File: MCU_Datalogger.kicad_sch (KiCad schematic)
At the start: 25 parts, among them U1 24LC1025, U2 DS1337S_, U3 24LC1025, U4 ATMEGA328P-AU, Y1 32.768 KHz, Y2 16MHz

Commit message: Completed Comment
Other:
- note added: "EEPROM"
- note added: "MCU ATMEGA328P"
- note added: "Mounting"
- note added: "RTC DS1377"
- moved on the sheet: BT1, C1, C2, C3, C4, C5, D1, D2, H1, H2, H3, H4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

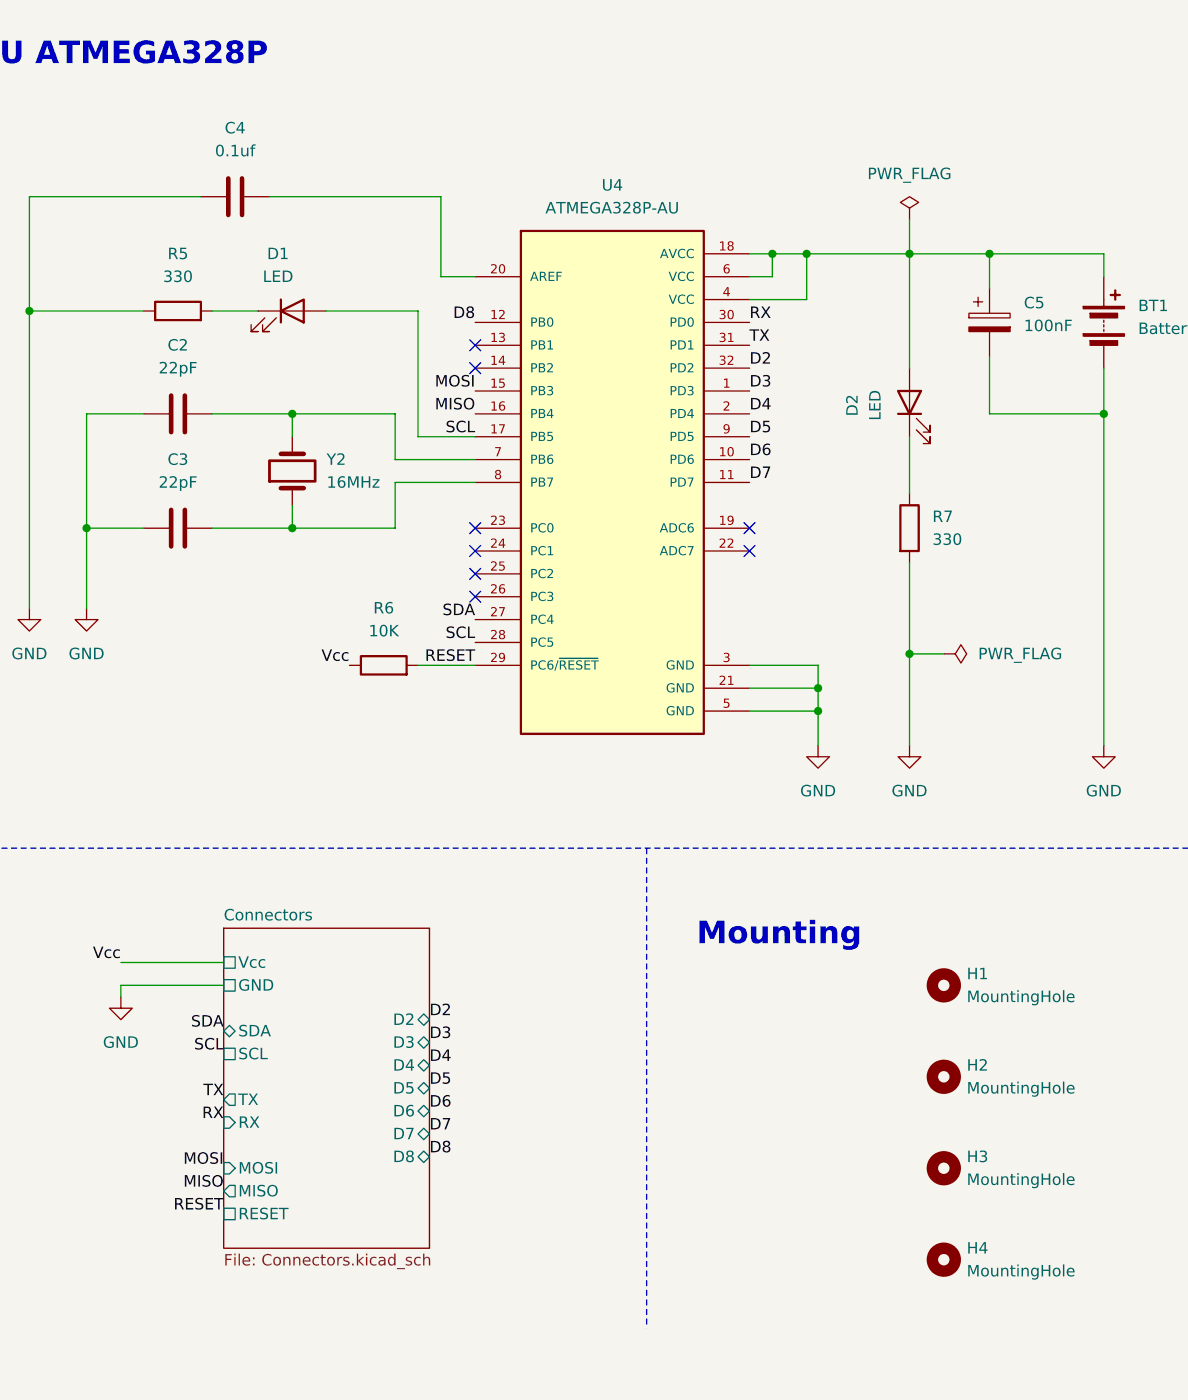
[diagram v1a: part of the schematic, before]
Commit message: Routing, GND Plane, Rework VCC Line and slick Screen complete
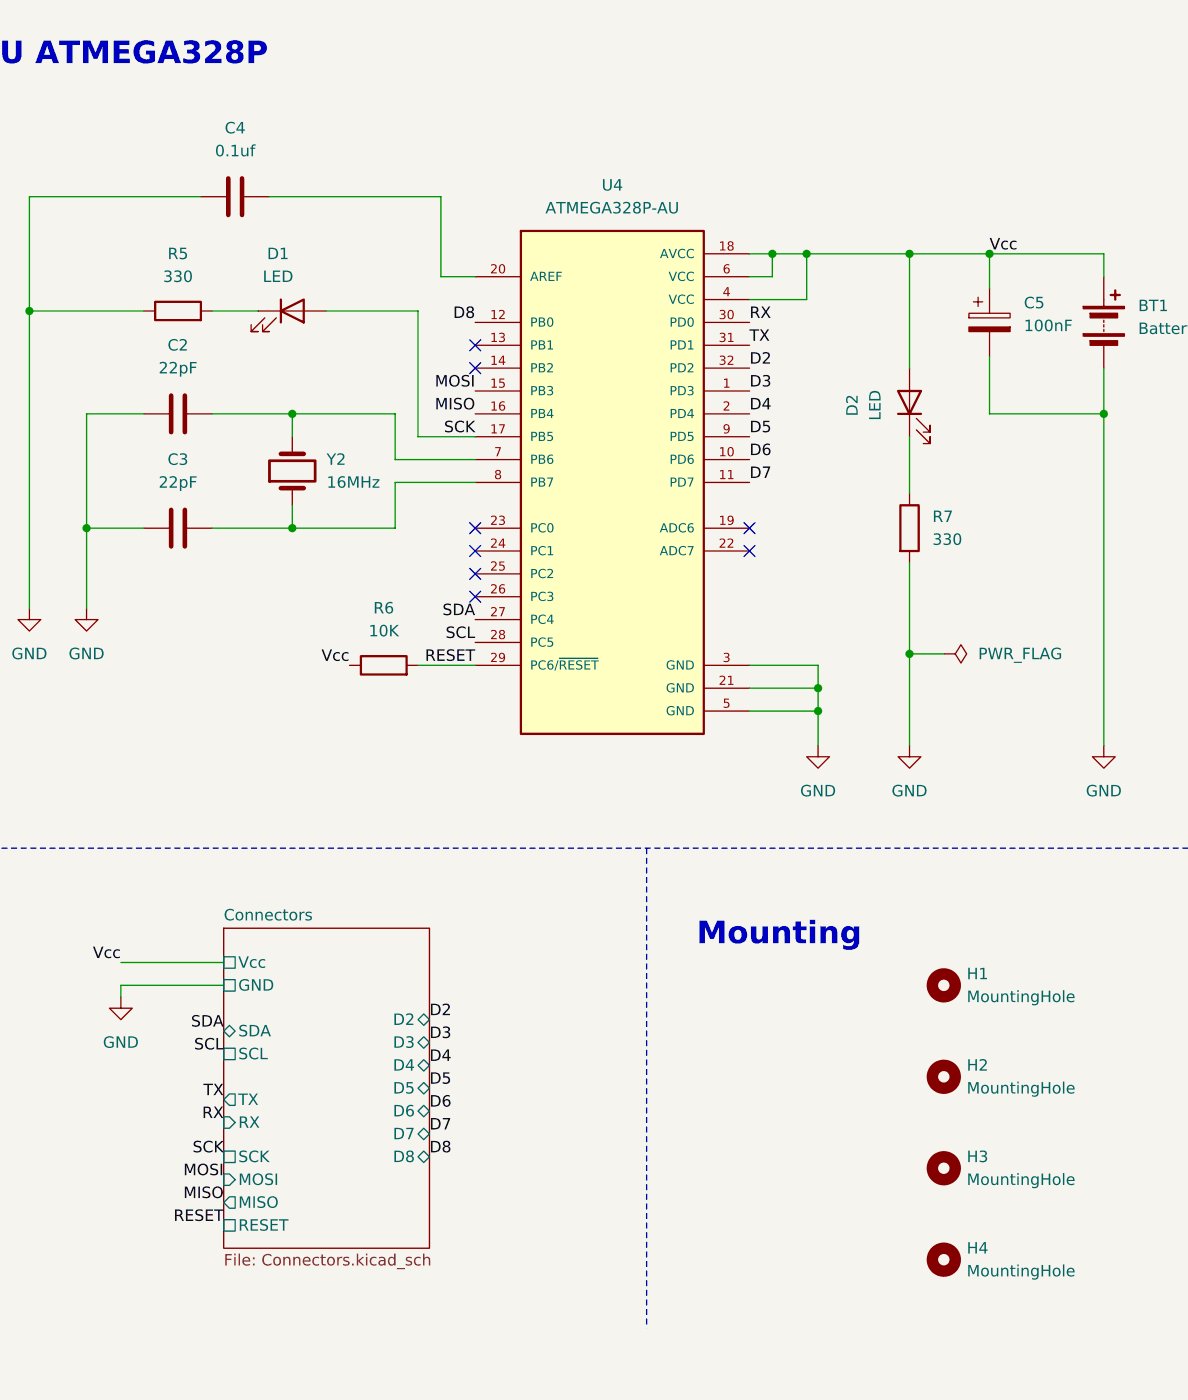
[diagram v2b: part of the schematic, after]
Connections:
- net SCL: no longer D1.2 (A), U4.17 (PB5)
- net Vcc: now also BT1.1 (+), C5.1, D2.2 (A), U4.18 (AVCC), U4.4 (VCC), U4.6 (VCC)
- new net SCK: D1.2 (A), U4.17 (PB5)
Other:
- sheet Connectors ports: added SCK; removed none
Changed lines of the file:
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@@
 	(wire
 		(pts
-			(xy 242.57 41.91) (xy 242.57 45.72)
-		)
-		(stroke
-			(width 0)
-			(type default)
-		)
-	)
-	(wire
-		(pts
 			(xy 74.93 144.78) (xy 74.93 152.4)
 		)
@@
 		)
 	)
+	(label "SCK"
+		(at 166.37 146.05 180)
+		(effects
+			(font
+				(size 1.27 1.27)
+			)
+			(justify right bottom)
+		)
+	)
 	(label "D8"
 		(at 189.23 146.05 0)
@@
 		)
 	)
+	(label "Vcc"
+		(at 251.46 45.72 0)
+		(effects
+			(font
+				(size 1.27 1.27)
+			)
+			(justify left bottom)
+		)
+	)
 	(label "SCL"
 		(at 64.77 142.24 0)
@@
 	)
 	(label "MOSI"
-		(at 166.37 147.32 180)
+		(at 166.37 148.59 180)
 		(effects
 			(font
@@
 	)
 	(label "RESET"
-		(at 166.37 152.4 180)
+		(at 166.37 153.67 180)
 		(effects
 			(font
@@
 		)
 	)
-	(label "SCL"
+	(label "SCK"
 		(at 194.31 66.04 180)
 		(effects
@@
 	)
 	(label "MISO"
-		(at 166.37 149.86 180)
+		(at 166.37 151.13 180)
 		(effects
 			(font
@@
 	)
 	(symbol
-		(lib_id "power:PWR_FLAG")
-		(at 242.57 41.91 0)
-		(unit 1)
-		(exclude_from_sim no)
-		(in_bom yes)
-		(on_board yes)
-		(dnp no)
-		(fields_autoplaced yes)
-		(property "Reference" "#FLG01"
-			(at 242.57 40.005 0)
-			(effects
-				(font
-					(size 1.27 1.27)
-				)
-				(hide yes)
-			)
-		)
-		(property "Value" "PWR_FLAG"
-			(at 242.57 36.83 0)
-			(effects
-				(font
-					(size 1.27 1.27)
-				)
-			)
-		)
-		(property "Footprint" ""
-			(at 242.57 41.91 0)
-			(effects
-				(font
-					(size 1.27 1.27)
-				)
-				(hide yes)
-			)
-		)
-		(property "Datasheet" "~"
-			(at 242.57 41.91 0)
-			(effects
-				(font
-					(size 1.27 1.27)
-				)
-				(hide yes)
-			)
-		)
-		(property "Description" "Special symbol for telling ERC where power comes from"
-			(at 242.57 41.91 0)
-			(effects
-				(font
-					(size 1.27 1.27)
-				)
-				(hide yes)
-			)
-		)
-		(pin "1"
-		)
-		(instances
-			(project ""
-				(path "/d11b8ef8-3bec-4edf-bf58-e6d313bf30d2"
-					(reference "#FLG01")
-					(unit 1)
-				)
-			)
-		)
-	)
-	(symbol
 		(lib_id "Device:Crystal")
 		(at 173.99 69.85 90)
@@
 		)
 		(pin "MISO" output
-			(at 166.37 149.86 180)
+			(at 166.37 151.13 180)
 			(effects
 				(font
@@
 		)
 		(pin "RESET" passive
-			(at 166.37 152.4 180)
+			(at 166.37 153.67 180)
 			(effects
 				(font
@@
 		)
 		(pin "MOSI" input
-			(at 166.37 147.32 180)
+			(at 166.37 148.59 180)
 			(effects
 				(font
@@
 			)
 		)
+		(pin "SCK" passive
+			(at 166.37 146.05 180)
+			(effects
+				(font
+					(size 1.27 1.27)
+				)
+				(justify left)
+			)
+		)
